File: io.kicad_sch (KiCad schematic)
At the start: 1 part, among them U1 STM32H723ZGTx

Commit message: I dont know whats going on here
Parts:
- added C123, C124: 2.2uF, symbol Device:C_Small
- added C125, C126: 10pF, symbol Device:C_Small
- added C146: 1uF, symbol Device:C_Small
- added C147: 100nF, symbol Device:C_Small
- added C85: 100nF, aprlprints:C_0603-noct, symbol Device:C_Small
- added F2: 500mA, Fuse:Fuse_0805_2012Metric, symbol Device:Fuse_Small
- added J8: USB_C_Receptacle_USB2.0_16P, Connector_USB:USB_C_Receptacle_HRO_TYPE-C-31-M-12, symbol Connector:USB_C_Receptacle_USB2.0_16P
- added J9: Conn_02x05_Odd_Even, Connector_PinHeader_2.54mm:PinHeader_2x05_P2.54mm_Vertical, symbol Connector_Generic:Conn_02x05_Odd_Even
- added R15, R16: 4.7k, aprlprints:R_0603-noct, symbol Device:R_Small_US
- added SW1: SKRPANE010, symbol Switch:SW_MEC_5E
- added unit 8 of U1
- added U8: USBLC6-2SC6, Package_TO_SOT_SMD:SOT-23-6, symbol Power_Protection:USBLC6-2SC6
- added Y1: 25 MHz, symbol Device:Crystal_GND24_Small
- U1: value STM32H723ZGTx -> STM32H723ZGT6
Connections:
- new net: C125.2, U1.24 (PH1), Y1.1
- new net: J8.B5 (CC2), R15.2
- new net: SW1.1, SW1.2, U1.25 (NRST)
- new net: C126.2, U1.23 (PH0), Y1.3
- new net: C85.1, F2.1, J8.A4 (VBUS), J8.A9 (VBUS), J8.B4 (VBUS), J8.B9 (VBUS), U8.5 (VBUS)
- new net: J8.A5 (CC1), R16.1
- new net: C124.2, U1.106 (VCAP)
- new net: C123.2, U1.71 (VCAP)
- new net +3.3V: C146.2, C147.2, J9.1 (Pin_1), U1.143 (PDR_ON), U1.32 (VREF+)
- new net +5V: F2.2
- new net GND: C123.1, C124.1, C125.1, C126.1, C146.1, C147.1, C85.2, J8.A1 (GND), J8.A12 (GND), J8.B1 (GND), J8.B12 (GND), J8.S1 (SHIELD), J9.3 (Pin_3), J9.5 (Pin_5), J9.9 (Pin_9), R15.1, R16.2, SW1.3 (K), SW1.4 (A), U1.138 (BOOT0), U8.2 (GND), Y1.2 (G), Y1.4 (G)
- new net SWCLK: J9.4 (Pin_4)
- new net SWDIO: J9.2 (Pin_2)
- new net USB_CONN_D+: J8.A6 (D+), J8.B6 (D+), U8.3 (I/O2)
- new net USB_CONN_D-: J8.A7 (D-), J8.B7 (D-), U8.1 (I/O1)
- new net USB_D+: U8.4 (I/O2)
- new net USB_D-: U8.6 (I/O1)
- new net ~{RST}: J9.10 (Pin_10)
- no-connect marks 0 -> 5
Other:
- note added: "Debug Header"
- note added: "Pinout in STM32CubeMX"
- note added: "RECHECK WHEN CRYSTAL IS PICKED"
- note added: "See AN4938"
- note added: "USB"

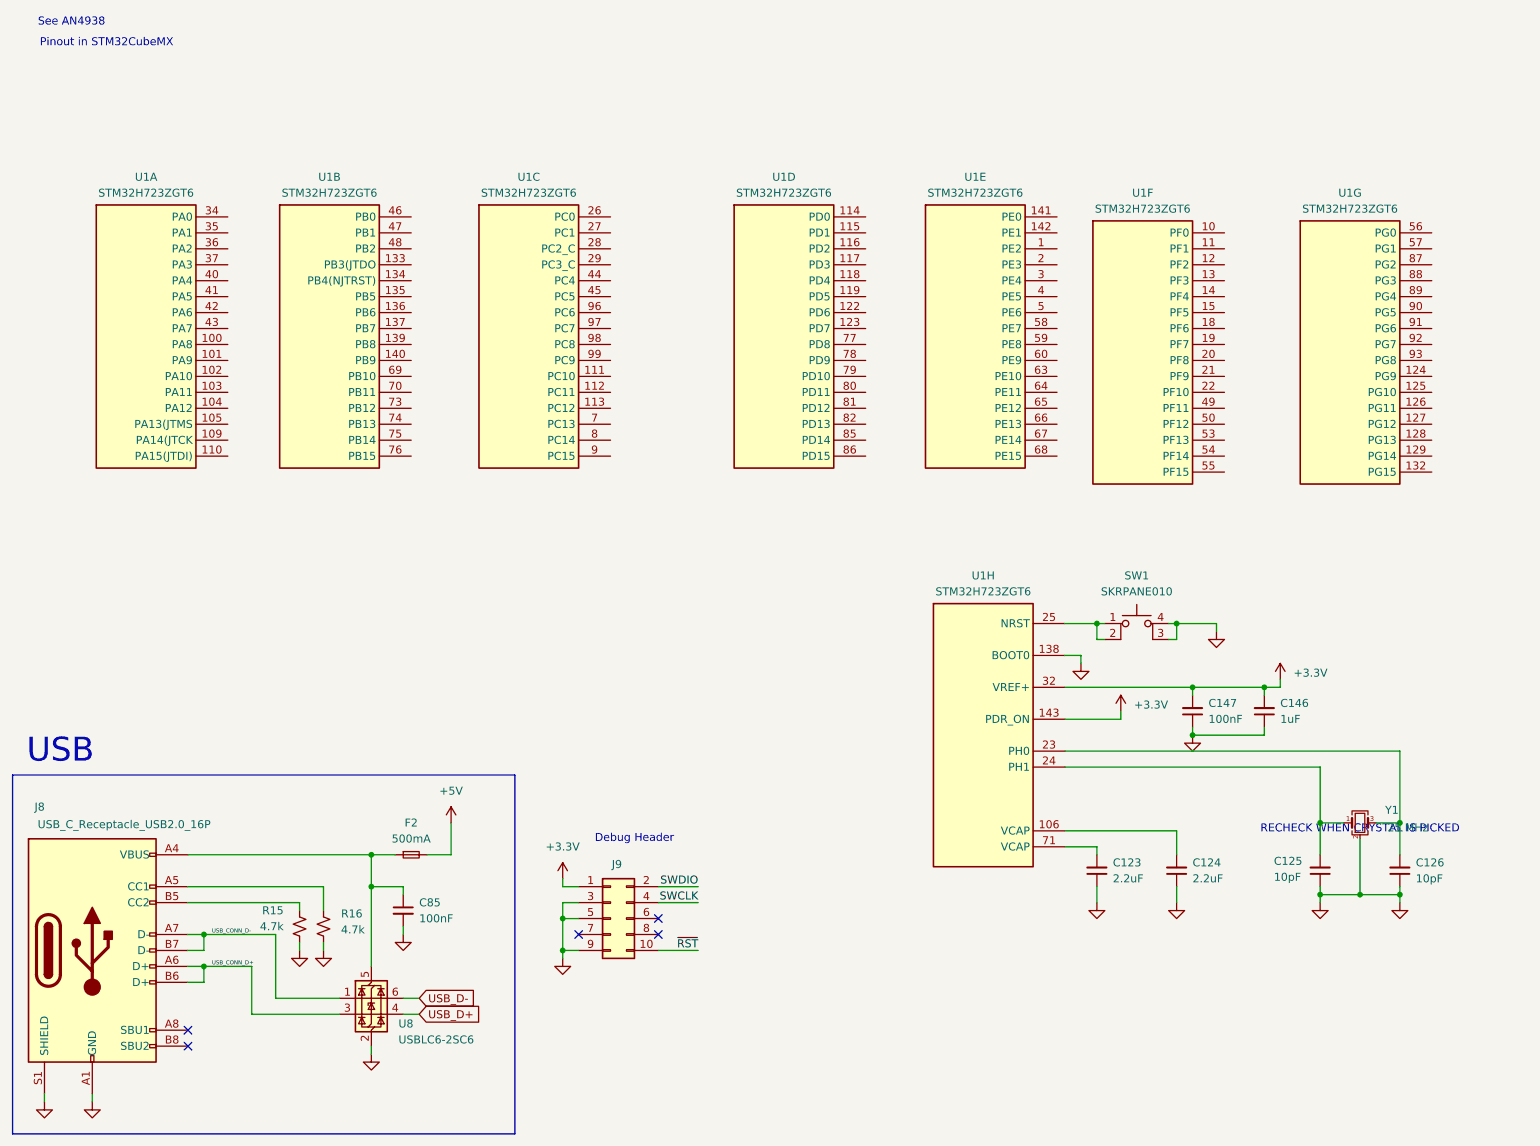
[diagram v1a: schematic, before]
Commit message: Soften scope, begin layout, reorganize sheets (still need to delete extras)
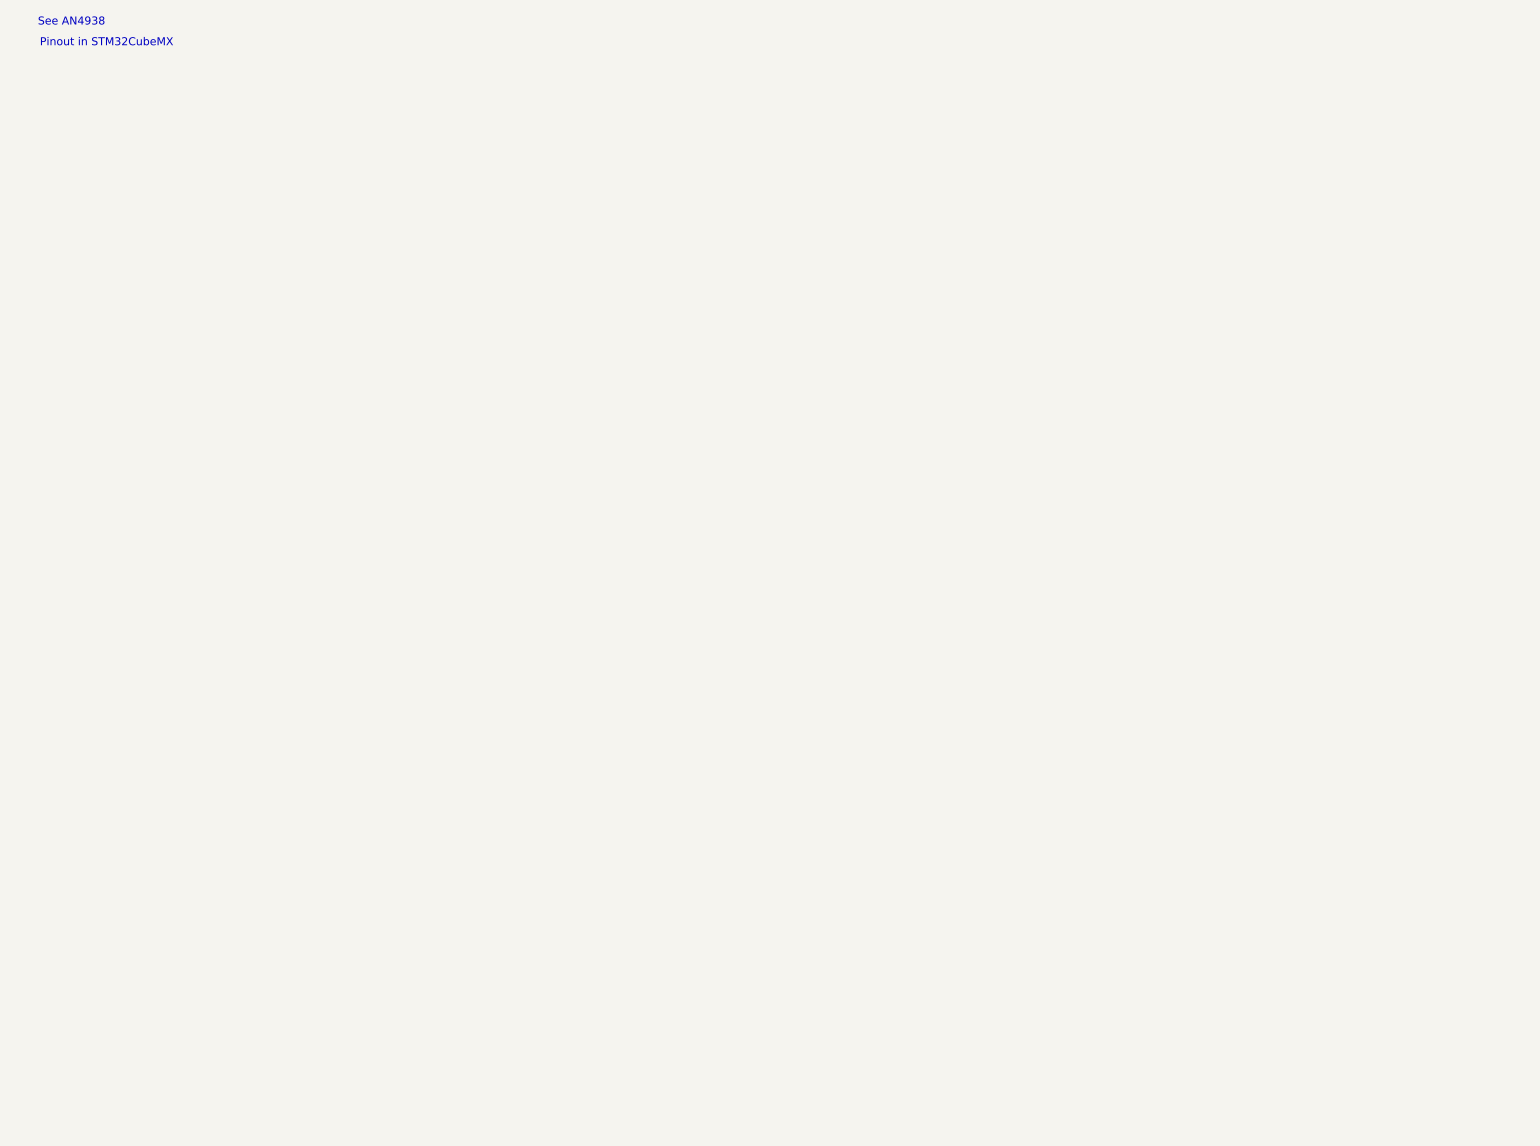
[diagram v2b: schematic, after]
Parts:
- removed C123, C124: 2.2uF, symbol Device:C_Small
- removed C125, C126: 10pF, symbol Device:C_Small
- removed C146: 1uF, symbol Device:C_Small
- removed C147: 100nF, symbol Device:C_Small
- removed C85: 100nF, aprlprints:C_0603-noct, symbol Device:C_Small
- removed F2: 500mA, Fuse:Fuse_0805_2012Metric, symbol Device:Fuse_Small
- removed J8: USB_C_Receptacle_USB2.0_16P, Connector_USB:USB_C_Receptacle_HRO_TYPE-C-31-M-12, symbol Connector:USB_C_Receptacle_USB2.0_16P
- removed J9: Conn_02x05_Odd_Even, Connector_PinHeader_2.54mm:PinHeader_2x05_P2.54mm_Vertical, symbol Connector_Generic:Conn_02x05_Odd_Even
- removed R15, R16: 4.7k, aprlprints:R_0603-noct, symbol Device:R_Small_US
- removed SW1: SKRPANE010, symbol Switch:SW_MEC_5E
- removed U1: STM32H723ZGT6, Package_QFP:LQFP-144_20x20mm_P0.5mm, symbol libserie:STM32H723ZGTx
- removed U8: USBLC6-2SC6, Package_TO_SOT_SMD:SOT-23-6, symbol Power_Protection:USBLC6-2SC6
- removed Y1: 25 MHz, symbol Device:Crystal_GND24_Small
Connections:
- no-connect marks 5 -> 0
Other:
- note removed: "Debug Header"
- note removed: "RECHECK WHEN CRYSTAL IS PICKED"
- note removed: "USB"
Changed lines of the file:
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@@
 		(company "Nolan and Kanin")
 	)
+	(text "Pinout in STM32CubeMX"
+		(exclude_from_sim no)
+		(at 34.036 25.654 0)
+		(effects
+			(font
+				(size 1.27 1.27)
+			)
+		)
+	)
+	(text "See AN4938"
+		(exclude_from_sim no)
+		(at 28.448 22.352 0)
+		(effects
+			(font
+				(size 1.27 1.27)
+			)
+		)
+	)
+)
